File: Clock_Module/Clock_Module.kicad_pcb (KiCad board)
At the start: 2 copper layers, 95.9 x 90.2 mm, 33 parts, among them J1 PC104, SW1 Switch, U1 74LS08, U2 74LS32, U3 74LS04, U4 LM555xN, U5 LM555xN, U6 LM555xN

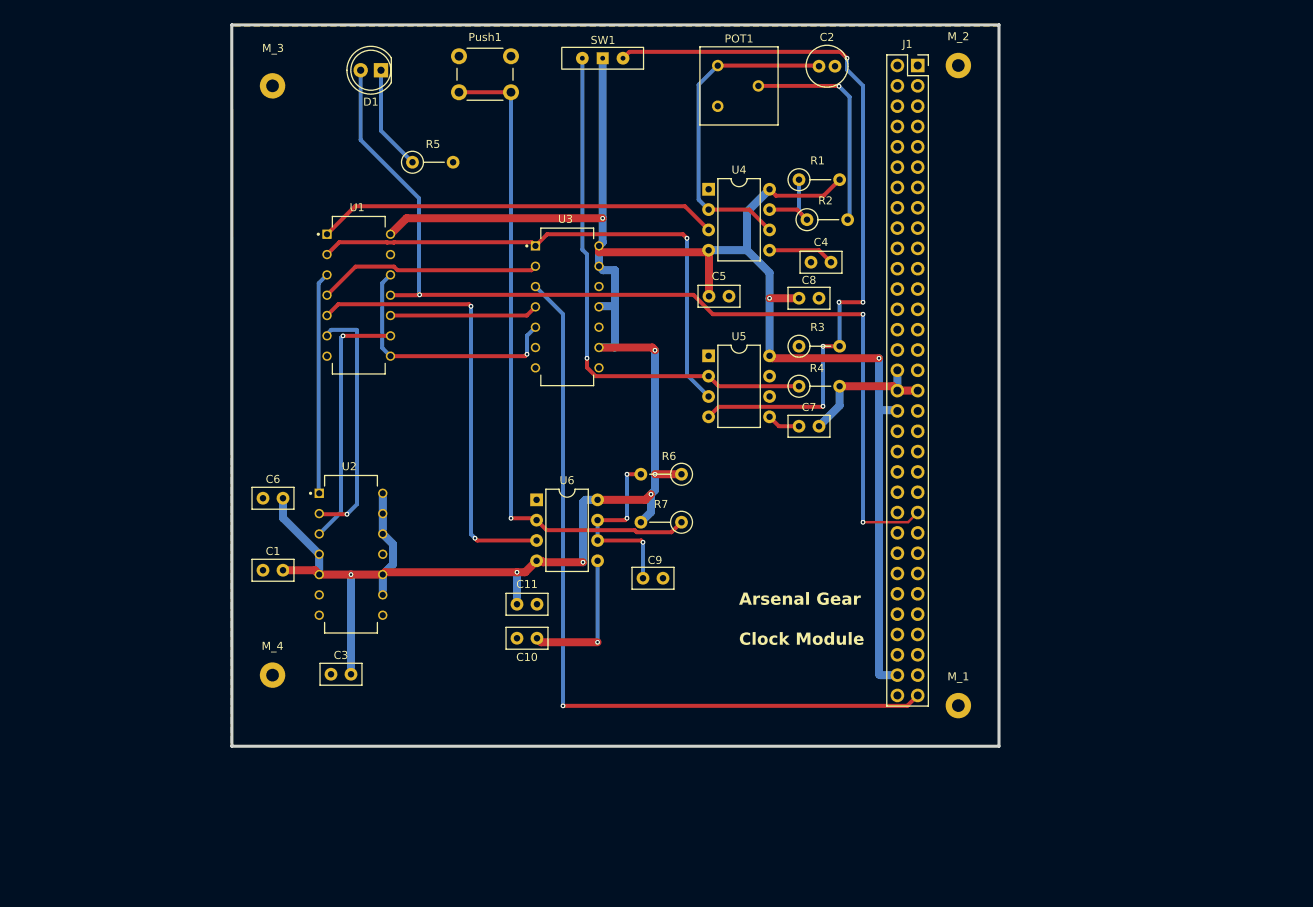
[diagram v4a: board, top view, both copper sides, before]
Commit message: Updated Clock Module Schematic, and moved Instruction Register to new board
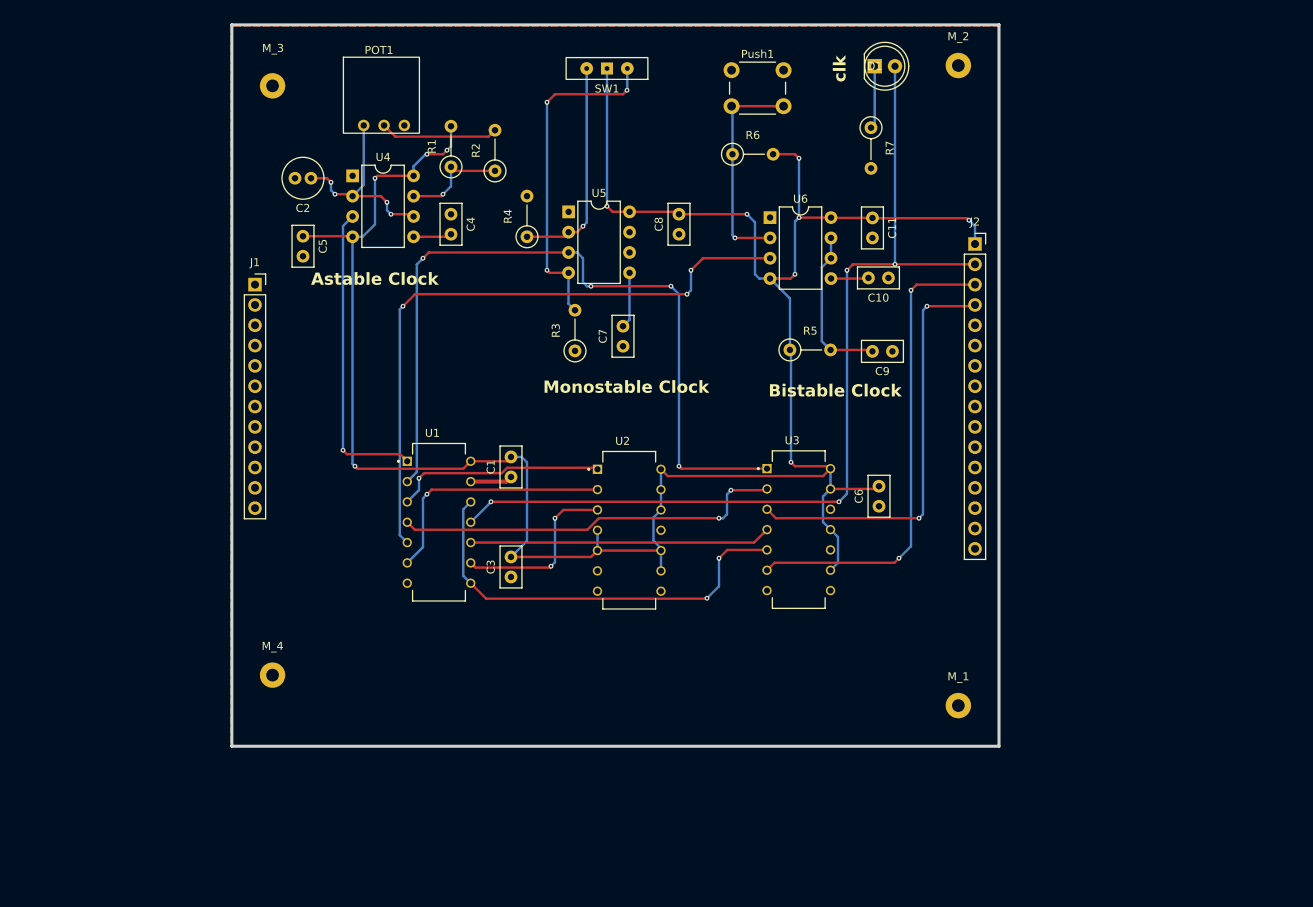
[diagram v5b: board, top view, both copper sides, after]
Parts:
- added J2: Conn_01x16, Connector_PinSocket_2.54mm:PinSocket_1x16_P2.54mm_Vertical, F.Cu at (174.8, 64.2)
- J1: value PC104 -> Conn_01x12; footprint Connector_PinSocket_2.54mm:PinSocket_2x32_P2.54mm_Vertical -> Connector_PinSocket_2.54mm:PinSocket_1x12_P2.54mm_Vertical
- POT1: footprint Potentiometer_THT:Potentiometer_Bourns_3386F_Vertical -> Potentiometer_THT:Potentiometer_Bourns_3266Y_Vertical
- R5: value 1K -> 1M
- R6: value 1M -> 1K
- moved J1 87.3 mm to (84.8, 69.3)
- moved C6 77.0 mm to (162.8, 97.0), turned to 90 degrees
- moved C11 65.6 mm to (162.0, 61.0), turned to -90 degrees
- moved C2 65.0 mm to (91.8, 56.0), turned to 180 degrees
- moved C10 64.7 mm to (164.0, 68.5), turned to 180 degrees
- moved D1 61.7 mm to (162.3, 42.0), turned to 0 degrees
- moved R7 54.7 mm to (161.8, 49.7), turned to -90 degrees
- moved R5 52.7 mm to (151.7, 77.5)
- moved C5 51.3 mm to (90.8, 63.2), turned to -90 degrees
- moved U6 45.8 mm to (149.2, 60.9)
- moved C4 45.4 mm to (109.3, 60.5), turned to -90 degrees
- moved U4 44.5 mm to (97.0, 55.7)
- moved R1 43.5 mm to (109.3, 54.6), turned to 90 degrees
- moved POT1 41.1 mm to (101.8, 42.5)
- moved R6 40.5 mm to (144.5, 53.0), turned to 0 degrees
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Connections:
- net /astable_out renamed /Clock/astable_out
- net /bistable_out renamed /Clock/bistable_out
- net /monostable_out renamed /Clock/monostable_out
- R5 pad 1: Net-(D1-K) -> 5V
- R5 pad 2: GND -> Net-(U6-DIS)
- R6 pad 1: 5V -> Net-(U6-TR)
- R6 pad 2: Net-(U6-DIS) -> 5V
- R7 pad 1: Net-(U6-TR) -> Net-(D1-K)
- R7 pad 2: 5V -> GND
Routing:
- net /~{CLK}: track 0.00 -> 59.5 mm, vias 0 -> 2
- net Net-(U6-TR): track 82.3 -> 27.5 mm
- net Net-(SW1-C): track 93.1 -> 42.2 mm, vias 5 -> 3
- net /halt: track 98.7 -> 52.4 mm, vias 1 -> 2
- net Net-(SW1-A): track 66.4 -> 27.5 mm
- net /Clock/bistable_out: track 67.6 -> 97.6 mm, vias 1 -> 4
- net 5V: track 318.6 -> 291.9 mm, vias 9 -> 11
- net /Clock/monostable_out: track 55.7 -> 79.9 mm, vias 2 -> 3
- net Net-(U1-Pad12): track 32.0 -> 53.3 mm, vias 1 -> 2
- net Net-(U1-Pad4): track 27.9 -> 48.9 mm, vias 0 -> 2
- net Net-(U1-Pad10): track 18.6 -> 37.7 mm
- net Net-(U4-THR): track 40.9 -> 25.8 mm, vias 0 -> 4
- net GND: track 19.1 -> 5.27 mm
- net Net-(U6-CV): track 18.0 -> 4.71 mm, vias 1 -> 0
- net Net-(POT1-Pad2): track 27.4 -> 14.8 mm, vias 1 -> 0
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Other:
- board text added: "Astable Clock"
- board text added: "Bistable Clock"
- board text added: "Monostable Clock"
- board text added: "clk"
- board text removed: "Arsenal Gear"
- board text removed: "Clock Module"

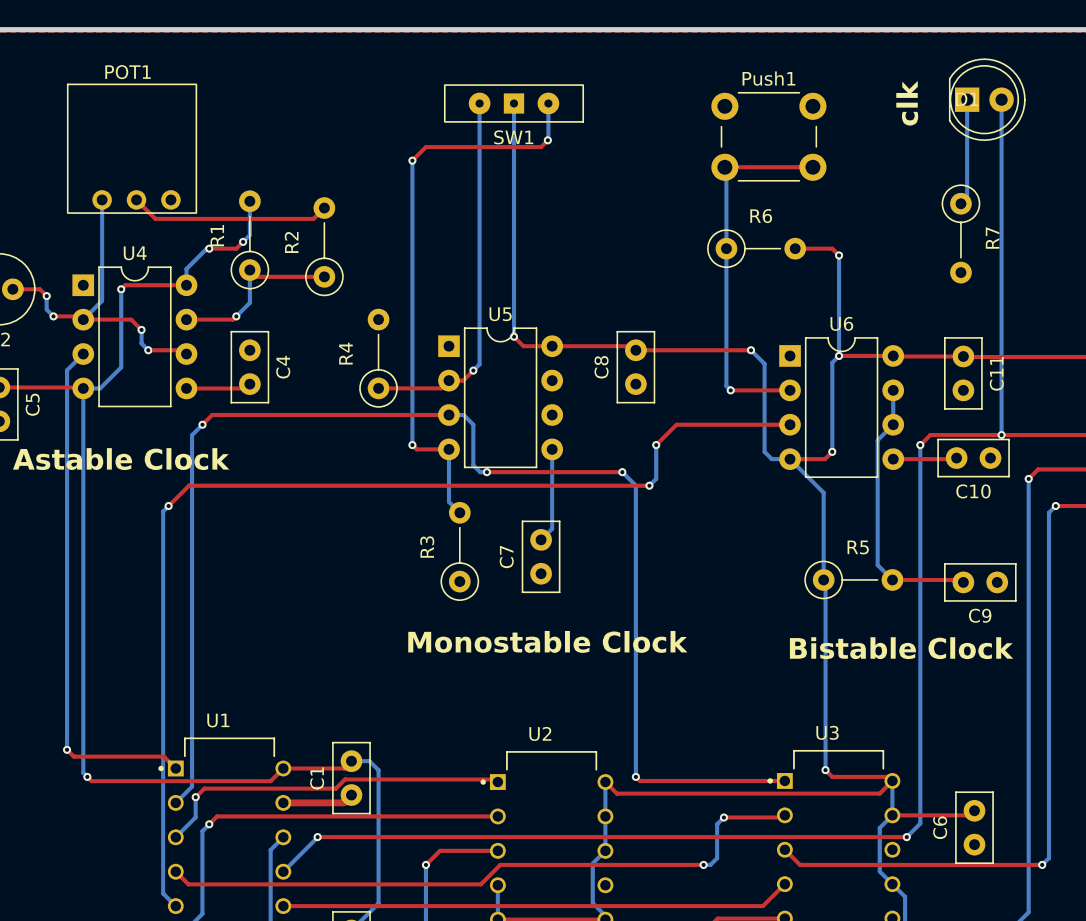
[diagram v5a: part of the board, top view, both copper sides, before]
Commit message: mostly routed IR, fixed logic issue in Clock Module
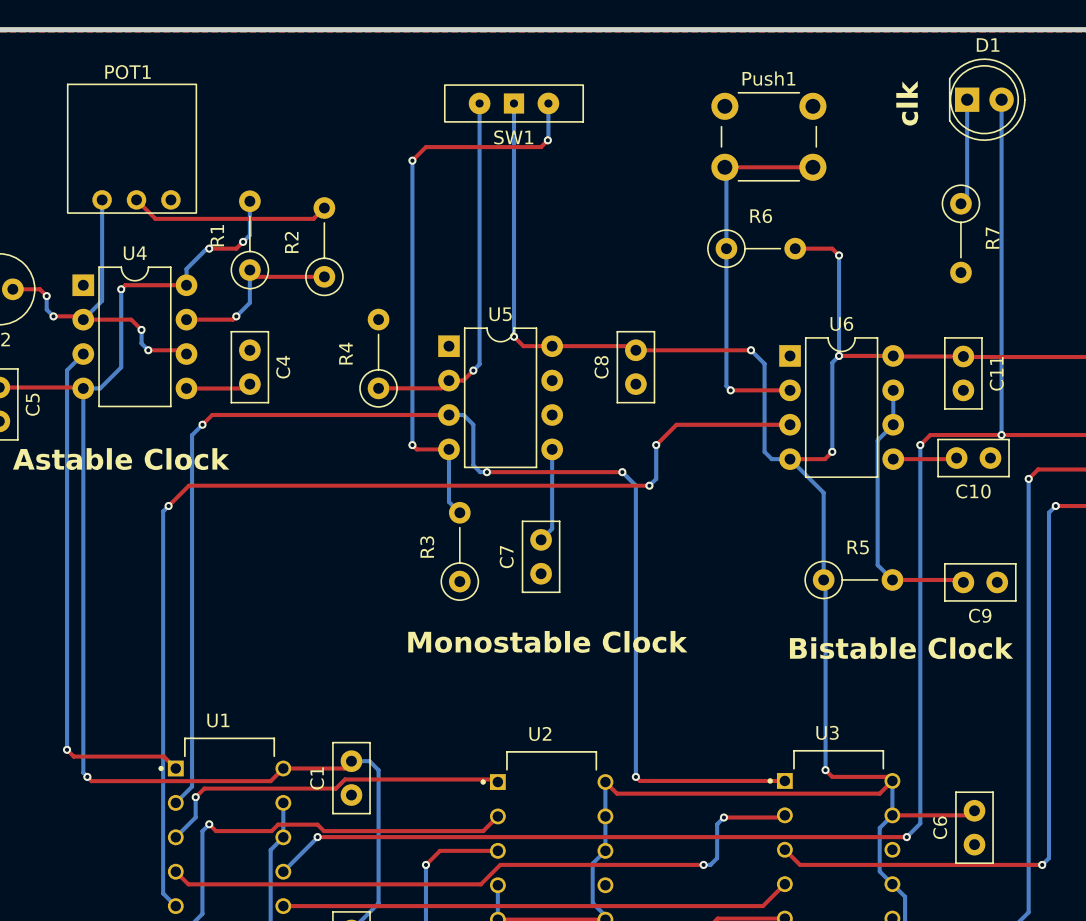
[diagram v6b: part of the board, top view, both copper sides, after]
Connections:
- U1 pad 13: GND -> Net-(U1-Pad12)
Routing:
- net GND: track 5.27 -> 0.00 mm
- net Net-(U1-Pad12): track 53.3 -> 55.9 mm
- net Net-(U1-Pad6): track 31.2 -> 32.0 mm
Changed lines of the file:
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@@
 		(tags "LED")
 		(property "Reference" "D1"
-			(at 0 0 0)
+			(at 1.54 -4 0)
 			(layer "F.SilkS")
 			(effects
@@
 	)
 	(footprint "Connector_PinSocket_2.54mm:PinSocket_1x12_P2.54mm_Vertical"
+		(locked yes)
 		(layer "F.Cu")
 		(at 84.8 69.3)
@@
 			(layers "*.Cu" "*.Mask")
 			(remove_unused_layers no)
-			(net 1 "GND")
+			(net 36 "Net-(U1-Pad12)")
 			(pintype "input")
 			(solder_mask_margin 0.102)
@@
 	)
 	(footprint "Connector_PinSocket_2.54mm:PinSocket_1x16_P2.54mm_Vertical"
+		(locked yes)
 		(layer "F.Cu")
 		(at 174.8 64.22)
@@
 	)
 	(segment
-		(start 111.77 93.92)
-		(end 116.22 93.92)
-		(width 0.5)
-		(layer "F.Cu")
-		(net 1)
-	)
-	(segment
-		(start 116.22 93.92)
-		(end 116.8 93.34)
-		(width 0.5)
-		(layer "F.Cu")
-		(net 1)
-	)
-	(segment
 		(start 114.3 96.445)
 		(end 157.8 96.445)
@@
 	)
 	(segment
-		(start 97.3 58.5)
-		(end 97.04 58.24)
-		(width 0.3)
-		(layer "F.Cu")
-		(net 13)
-	)
-	(segment
 		(start 104.34 60.5)
 		(end 104.62 60.78)
@@
 		(net 13)
 	)
-	(segment
-		(start 97.04 58.24)
-		(end 97 58.24)
-		(width 0.3)
-		(layer "F.Cu")
-		(net 13)
-	)
 	(via
 		(at 94.8 58)
@@
 	)
 	(segment
-		(start 106.88 94.92)
-		(end 127.61 94.92)
+		(start 110.90771 96)
+		(end 111.38271 95.525)
 		(width 0.3)
 		(layer "F.Cu")
@@
 	(segment
 		(start 106.3 95.5)
-		(end 106.88 94.92)
+		(end 106.8 96)
+		(width 0.3)
+		(layer "F.Cu")
+		(net 23)
+	)
+	(segment
+		(start 114.299239 95.525)
+		(end 114.774239 96)
+		(width 0.3)
+		(layer "F.Cu")
+		(net 23)
+	)
+	(segment
+		(start 126.53 96)
+		(end 127.61 94.92)
+		(width 0.3)
+		(layer "F.Cu")
+		(net 23)
+	)
+	(segment
+		(start 114.774239 96)
+		(end 126.53 96)
+		(width 0.3)
+		(layer "F.Cu")
+		(net 23)
+	)
+	(segment
+		(start 111.38271 95.525)
+		(end 114.299239 95.525)
+		(width 0.3)
+		(layer "F.Cu")
+		(net 23)
+	)
+	(segment
+		(start 106.8 96)
+		(end 110.90771 96)
 		(width 0.3)
 		(layer "F.Cu")
@@
 		(width 0.3)
 		(layer "B.Cu")
+		(net 36)
+	)
+	(segment
+		(start 111.77 93.92)
+		(end 111.77 96.46)
+		(width 0.3)
+		(layer "B.Cu")

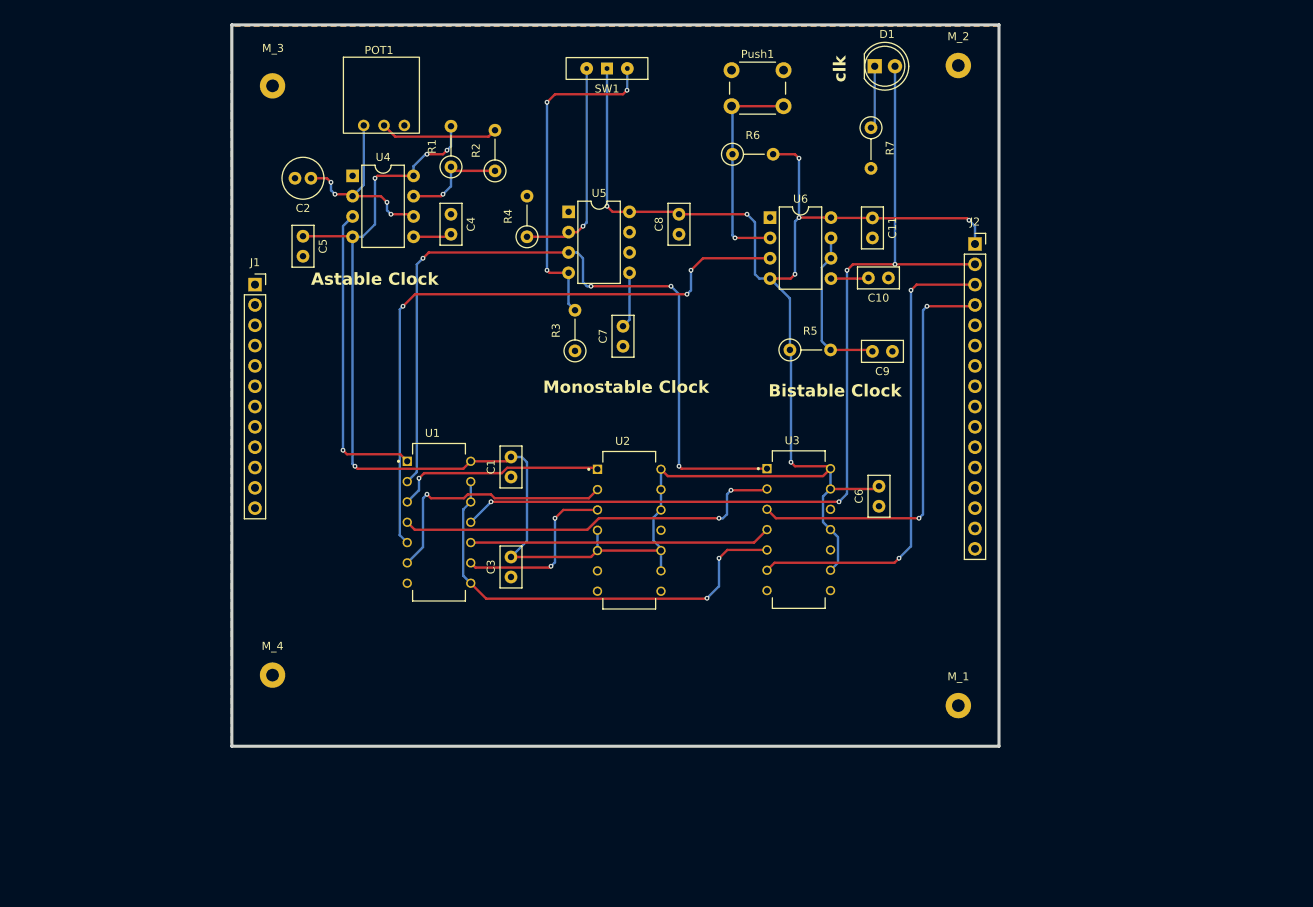
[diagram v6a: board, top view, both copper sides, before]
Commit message: returning to pc104 standard
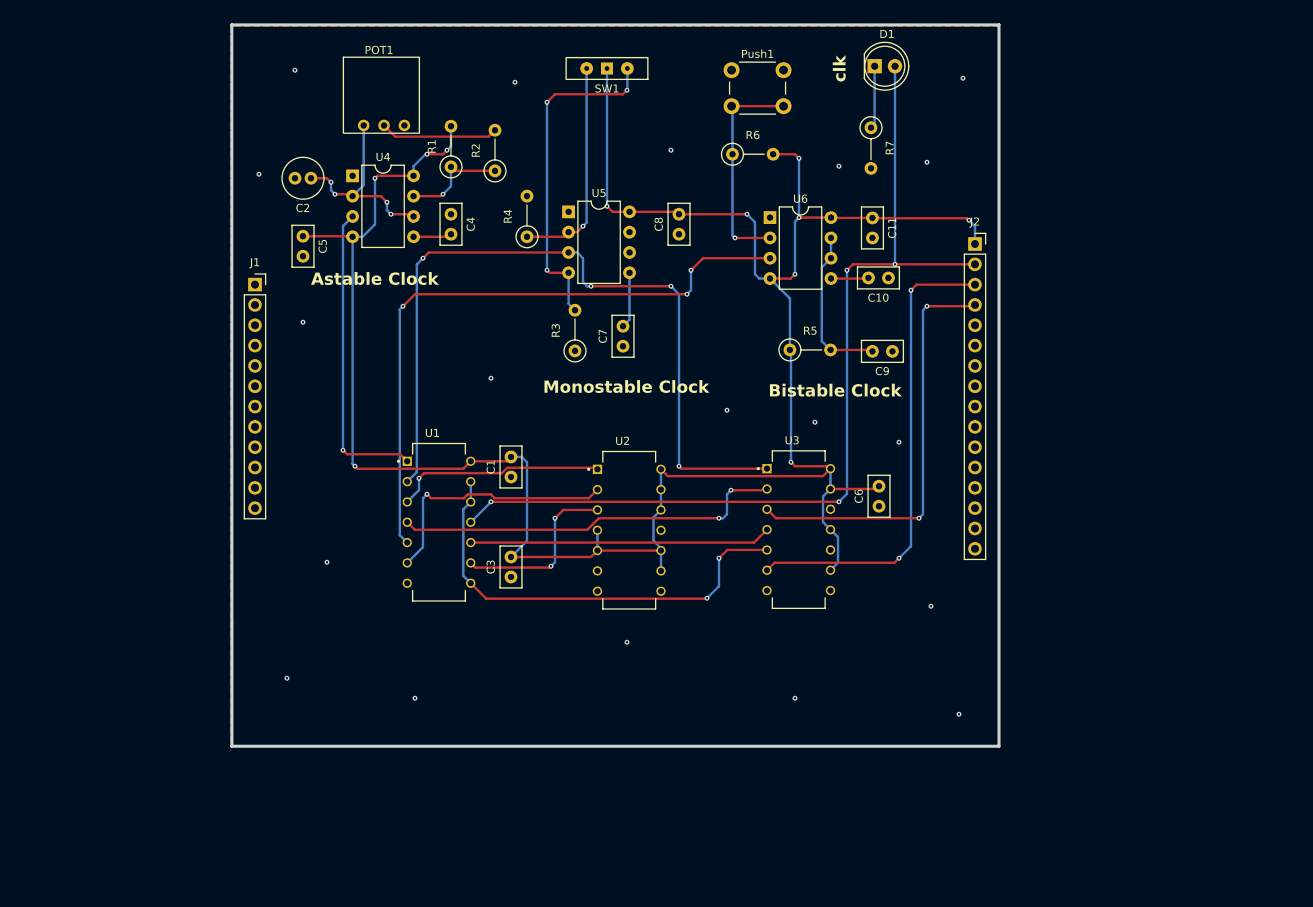
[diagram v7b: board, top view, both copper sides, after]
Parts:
- removed M_1, M_2, M_3, M_4: MountingHole_2.5mm_Pad, MountingHole:MountingHole_2.5mm_Pad
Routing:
- net GND: vias 0 -> 19
